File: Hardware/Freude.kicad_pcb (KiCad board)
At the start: 4 copper layers, 30 parts, among them J1 Conn_01x06_Female, J2 Conn_01x05_Female, J3 Conn_01x06_Female, J4 Conn_01x04_Female, J5 Conn_01x04_Female, J6 Conn_01x04_Male, U1 IQS572, U2 STM32L432KBUx, X1 Custom_Touchpad, Y1 Crystal_GND24

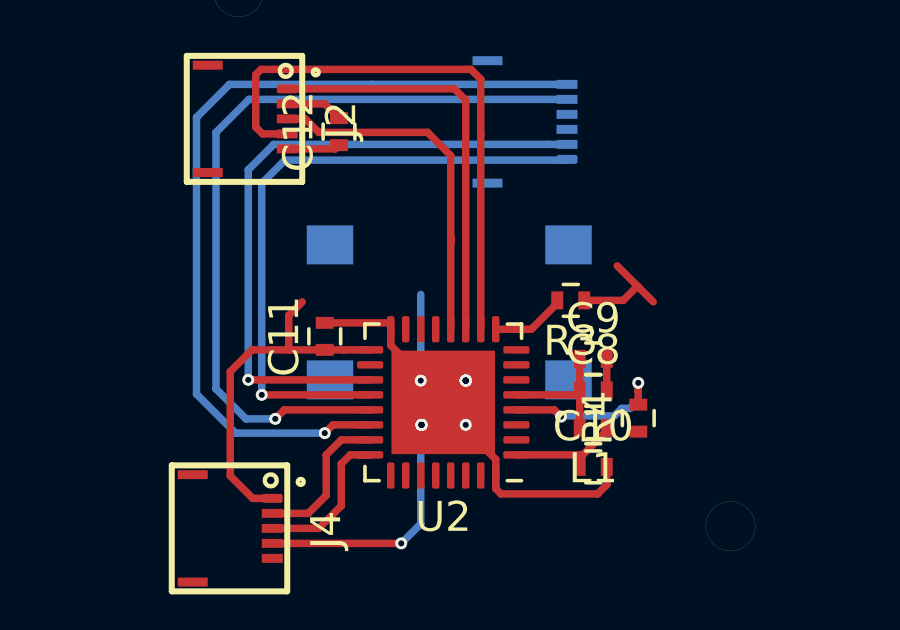
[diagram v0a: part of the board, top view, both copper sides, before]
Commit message: create part B3FS-1015p include 3d file. Add to PCB
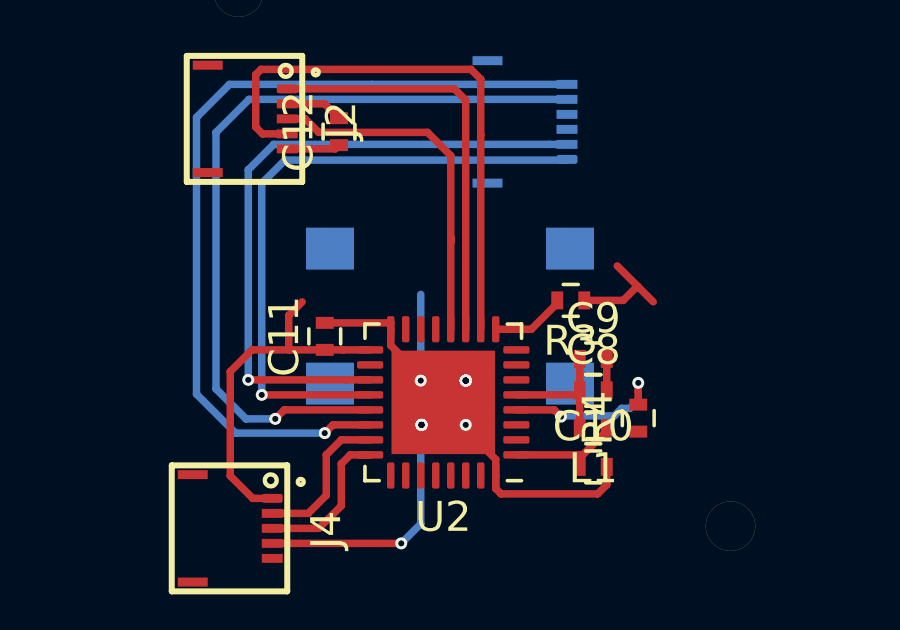
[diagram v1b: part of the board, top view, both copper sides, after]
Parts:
- removed the REF** at (200.7, 79.7)
- added REF**: B3FS-1015P, .pretty:B3FS-1015P, B.Cu at (200.7, 79.8)
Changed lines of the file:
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@@
     (35 F.Paste user hide)
     (37 F.SilkS user)
-    (39 F.Mask user)
+    (39 F.Mask user hide)
     (40 Dwgs.User user)
     (41 Cmts.User user)
@@
     (43 Eco2.User user)
     (44 Edge.Cuts user)
-    (45 Margin user)
+    (45 Margin user hide)
     (46 B.CrtYd user)
-    (47 F.CrtYd user)
+    (47 F.CrtYd user hide)
     (49 F.Fab user hide)
   )
@@
     )
   )
-  (module digikey-footprints:Switch_Tactile_SMD_6x6mm_PTS645 (layer B.Cu)
-    (at 200.7 79.7 180)
-    (descr http://www.ckswitches.com/media/1471/pts645.pdf)
-    (fp_text reference REF** (at 0 4.27 180) (layer B.SilkS)
-      (effects (font (size 1 1) (thickness 0.15)) (justify mirror))
-    )
-    (fp_text value Switch_Tactile_SMD_6x6mm_PTS645 (at 0 -4.5 180) (layer B.Fab)
-      (effects (font (size 1 1) (thickness 0.15)) (justify mirror))
-    )
-    (fp_line (start -3 3) (end 3 3) (layer B.Fab) (width 0.1))
-    (fp_line (start -3 -3) (end 3 -3) (layer B.Fab) (width 0.1))
-    (fp_line (start -3 3) (end -3 -3) (layer B.Fab) (width 0.1))
-    (fp_line (start 3 -3) (end 3 3) (layer B.Fab) (width 0.1))
-    (fp_line (start -3.1 0) (end -3.1 0.5) (layer B.SilkS) (width 0.1))
-    (fp_line (start -3.1 0) (end -3.1 -0.5) (layer B.SilkS) (width 0.1))
-    (fp_line (start 3.1 0) (end 3.1 0.5) (layer B.SilkS) (width 0.1))
-    (fp_line (start 3.1 0) (end 3.1 -0.5) (layer B.SilkS) (width 0.1))
-    (fp_line (start 0 -3.1) (end -0.5 -3.1) (layer B.SilkS) (width 0.1))
-    (fp_line (start 0 -3.1) (end 0.5 -3.1) (layer B.SilkS) (width 0.1))
-    (fp_line (start 0 3.1) (end 0.5 3.1) (layer B.SilkS) (width 0.1))
-    (fp_line (start 0 3.1) (end -0.5 3.1) (layer B.SilkS) (width 0.1))
-    (fp_line (start -3.4 3) (end -4.6 3) (layer B.SilkS) (width 0.1))
-    (fp_line (start -3.1 3) (end -3.4 3) (layer B.SilkS) (width 0.1))
-    (fp_line (start -3.1 3.1) (end -3.1 3) (layer B.SilkS) (width 0.1))
-    (fp_line (start -2.6 3.1) (end -3.1 3.1) (layer B.SilkS) (width 0.1))
-    (fp_text user %R (at 0 0 180) (layer B.Fab)
-      (effects (font (size 1 1) (thickness 0.15)) (justify mirror))
-    )
-    (fp_line (start 5 3.25) (end 5 -3.25) (layer B.CrtYd) (width 0.05))
-    (fp_line (start 5 3.25) (end -5 3.25) (layer B.CrtYd) (width 0.05))
-    (fp_line (start 5 -3.25) (end -5 -3.25) (layer B.CrtYd) (width 0.05))
-    (fp_line (start -5 3.25) (end -5 -3.25) (layer B.CrtYd) (width 0.05))
-    (pad 4 smd rect (at 3.975 -2.25 180) (size 1.55 1.3) (layers B.Cu B.Paste B.Mask))
-    (pad 3 smd rect (at -3.975 -2.25 180) (size 1.55 1.3) (layers B.Cu B.Paste B.Mask))
-    (pad 2 smd rect (at 3.975 2.25 180) (size 1.55 1.3) (layers B.Cu B.Paste B.Mask))
-    (pad 1 smd rect (at -3.975 2.25 180) (size 1.55 1.3) (layers B.Cu B.Paste B.Mask))
-  )
   (module Resistors_SMD:R_0402 (layer F.Cu)
     (at 207 83.225 90)
@@
     )
   )
+  (module .pretty:B3FS-1015P (layer B.Cu)
+    (at 200.725 79.825)
+    (fp_text reference REF** (at 0 -0.5) (layer B.SilkS)
+      (effects (font (size 1 1) (thickness 0.15)) (justify mirror))
+    )
+    (fp_text value B3FS-1015P (at 0 0.5) (layer B.Fab)
+      (effects (font (size 1 1) (thickness 0.15)) (justify mirror))
+    )
+    (fp_line (start -0.5 0) (end 0.5 0) (layer B.CrtYd) (width 0.2))
+    (fp_line (start 0 0.5) (end 0 -0.5) (layer B.CrtYd) (width 0.2))
+    (fp_line (start -3.15 -1.2) (end -3.15 1.2) (layer B.SilkS) (width 0.2))
+    (fp_line (start -2.8 3) (end 2.8 3) (layer B.SilkS) (width 0.2))
+    (fp_line (start 3.15 -1.2) (end 3.15 1.2) (layer B.SilkS) (width 0.2))
+    (fp_line (start -2.8 -3) (end 2.8 -3) (layer B.SilkS) (width 0.2))
+    (fp_line (start -3.15 -3) (end -3.15 3) (layer B.CrtYd) (width 0.2))
+    (fp_line (start 3.15 -3) (end 3.15 3) (layer B.CrtYd) (width 0.2))
+    (fp_line (start -3.15 -3) (end 3.15 -3) (layer B.CrtYd) (width 0.2))
+    (fp_line (start -3.15 3) (end 3.15 3) (layer B.CrtYd) (width 0.2))
+    (pad 4 smd rect (at -4 2.25) (size 1.6 1.4) (layers B.Cu B.Paste B.Mask))
+    (pad 3 smd rect (at 4 2.25) (size 1.6 1.4) (layers B.Cu B.Paste B.Mask))
+    (pad 2 smd rect (at -4 -2.25) (size 1.6 1.4) (layers B.Cu B.Paste B.Mask))
+    (pad 1 smd rect (at 4 -2.25) (size 1.6 1.4) (layers B.Cu B.Paste B.Mask))
+    (model ${KIPRJMOD}/.pretty/B3FS_1000.step
+      (at (xyz 0 0 0))
+      (scale (xyz 1 1 1))
+      (rotate (xyz -90 0 0))
+    )
+  )

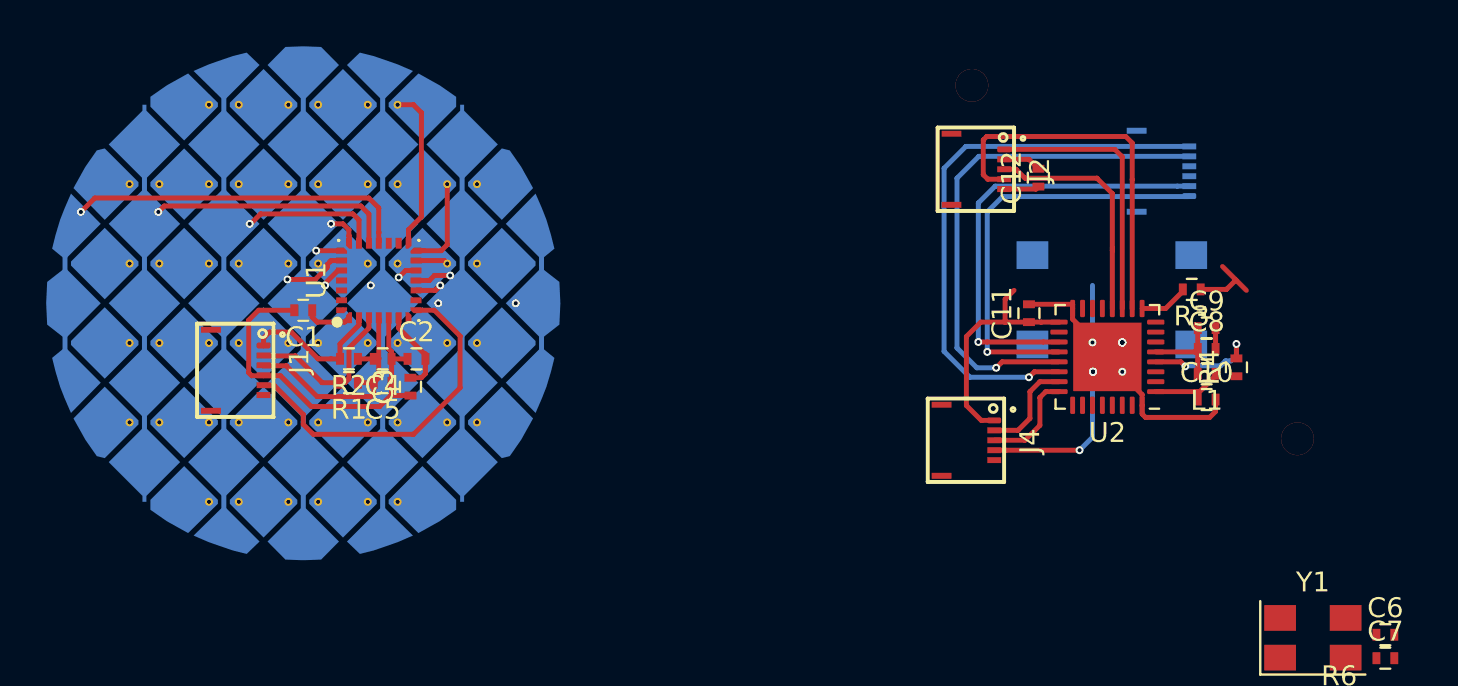
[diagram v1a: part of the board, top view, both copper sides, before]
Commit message: define boards edges
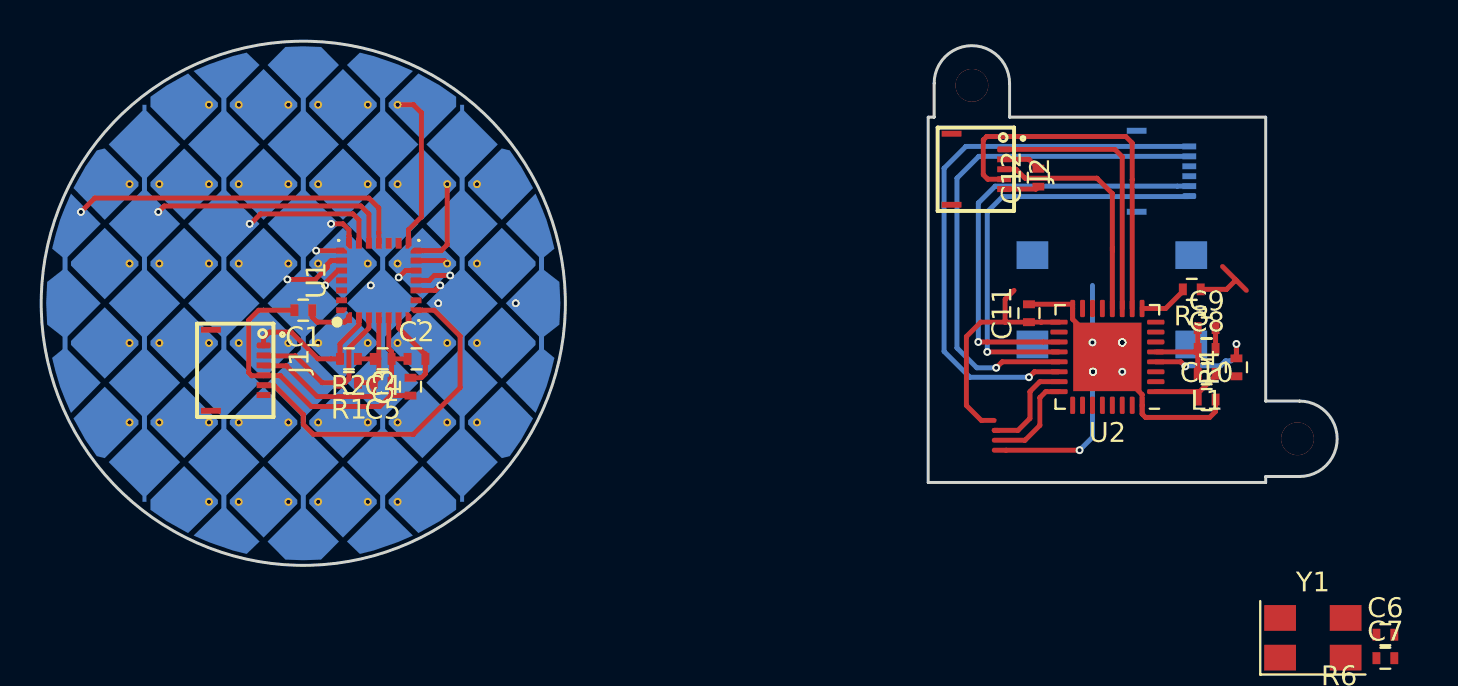
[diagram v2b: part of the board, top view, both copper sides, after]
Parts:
- removed J4: Conn_01x04_Female, .pretty:503480-0500
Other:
- board outline added: 65.3 x 26.4 mm
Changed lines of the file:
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@@
   (general
     (thickness 1.6)
-    (drawings 15)
+    (drawings 29)
     (tracks 329)
     (zones 0)
-    (modules 30)
+    (modules 29)
     (nets 63)
   )
@@
     (33 F.Adhes user hide)
     (35 F.Paste user hide)
-    (37 F.SilkS user)
+    (37 F.SilkS user hide)
     (39 F.Mask user hide)
     (40 Dwgs.User user)
@@
   )
   (module .pretty:503480-0500 (layer F.Cu)
-    (at 194.8 86.9 270)
-    (fp_text reference J4 (at 0.05 -1.8 270) (layer F.SilkS)
-      (effects (font (size 1 1) (thickness 0.15)))
-    )
-    (fp_text value Conn_01x04_Female (at 0 -0.5 270) (layer F.Fab)
-      (effects (font (size 1 1) (thickness 0.15)))
-    )
-    (fp_line (start -2.05 3.25) (end -2.05 -0.45) (layer F.CrtYd) (width 0.2))
-    (fp_line (start 2.05 3.25) (end -2.05 3.25) (layer F.CrtYd) (width 0.2))
-    (fp_line (start 2.05 -0.45) (end 2.05 3.25) (layer F.CrtYd) (width 0.2))
-    (fp_line (start -2.05 -0.45) (end 2.05 -0.45) (layer F.CrtYd) (width 0.2))
-    (fp_line (start 0 1.675) (end 0 2.675) (layer F.CrtYd) (width 0.2))
-    (fp_line (start -0.5 2.175) (end 0.5 2.175) (layer F.CrtYd) (width 0.2))
-    (fp_circle (center -1.6 0.05) (end -1.529289 0.05) (layer F.SilkS) (width 0.4))
-    (fp_circle (center -1.55 -0.95) (end -1.5 -0.9) (layer F.SilkS) (width 0.2))
-    (fp_line (start 2.1 3.35) (end 2.1 -0.5) (layer F.SilkS) (width 0.2))
-    (fp_line (start -2.1 -0.5) (end 2.1 -0.5) (layer F.SilkS) (width 0.2))
-    (fp_line (start -2.1 3.35) (end -2.1 -0.5) (layer F.SilkS) (width 0.2))
-    (fp_line (start -2.1 3.35) (end 2.1 3.35) (layer F.SilkS) (width 0.2))
-    (pad 0 smd rect (at 1.79 2.65 270) (size 0.3 1) (layers F.Cu F.Paste F.Mask))
-    (pad 0 smd rect (at -1.79 2.65 270) (size 0.3 1) (layers F.Cu F.Paste F.Mask))
-    (pad 5 smd rect (at 1 0 270) (size 0.3 0.7) (layers F.Cu F.Paste F.Mask))
-    (pad 4 smd rect (at 0.5 0 270) (size 0.3 0.7) (layers F.Cu F.Paste F.Mask)
-      (net 16 GND))
-    (pad 3 smd rect (at 0 0 270) (size 0.3 0.7) (layers F.Cu F.Paste F.Mask)
-      (net 42 /SWCLK))
-    (pad 2 smd rect (at -0.5 0 270) (size 0.3 0.7) (layers F.Cu F.Paste F.Mask)
-      (net 41 /SWDIO))
-    (pad 1 smd roundrect (at -1 0 270) (size 0.3 0.7) (layers F.Cu F.Paste F.Mask) (roundrect_rratio 0.25)
-      (net 15 +3V3))
-  )
-  (module .pretty:503480-0500 (layer F.Cu)
     (at 195.3 73.25 270)
     (fp_text reference J2 (at 0.05 -1.8 270) (layer F.SilkS)
@@
     )
   )
+  (gr_circle (center 160 80) (end 160 66.8) (layer Edge.Cuts) (width 0.15))
+  (gr_line (start 191.475 70.625) (end 191.475 89.025) (layer Edge.Cuts) (width 0.15))
+  (gr_line (start 191.775 70.625) (end 191.475 70.625) (layer Edge.Cuts) (width 0.15))
+  (gr_line (start 191.775 70.625) (end 191.775 68.925) (layer Edge.Cuts) (width 0.15))
+  (gr_arc (start 193.675 68.925) (end 195.575 68.925) (angle -180) (layer Edge.Cuts) (width 0.15))
+  (gr_line (start 195.575 70.625) (end 195.575 68.925) (layer Edge.Cuts) (width 0.15))
+  (gr_line (start 208.475 70.625) (end 195.575 70.625) (layer Edge.Cuts) (width 0.15))
+  (gr_line (start 208.475 84.925) (end 208.475 70.625) (layer Edge.Cuts) (width 0.15))
+  (gr_line (start 208.475 84.925) (end 210.175 84.925) (layer Edge.Cuts) (width 0.15))
+  (gr_arc (start 210.175 86.825) (end 210.175 88.725) (angle -180) (layer Edge.Cuts) (width 0.15))
+  (gr_line (start 208.475 88.725) (end 210.175 88.725) (layer Edge.Cuts) (width 0.15))
+  (gr_line (start 208.475 89.025) (end 208.475 88.725) (layer Edge.Cuts) (width 0.15))
+  (gr_line (start 208.45 89.025) (end 208.475 89.025) (layer Edge.Cuts) (width 0.15))
+  (gr_line (start 191.475 89.025) (end 208.45 89.025) (layer Edge.Cuts) (width 0.15))
   (gr_circle (center 160 80) (end 173 80) (layer Dwgs.User) (width 0.2))
   (gr_circle (center 160 80) (end 173 80) (layer Dwgs.User) (width 0.2))

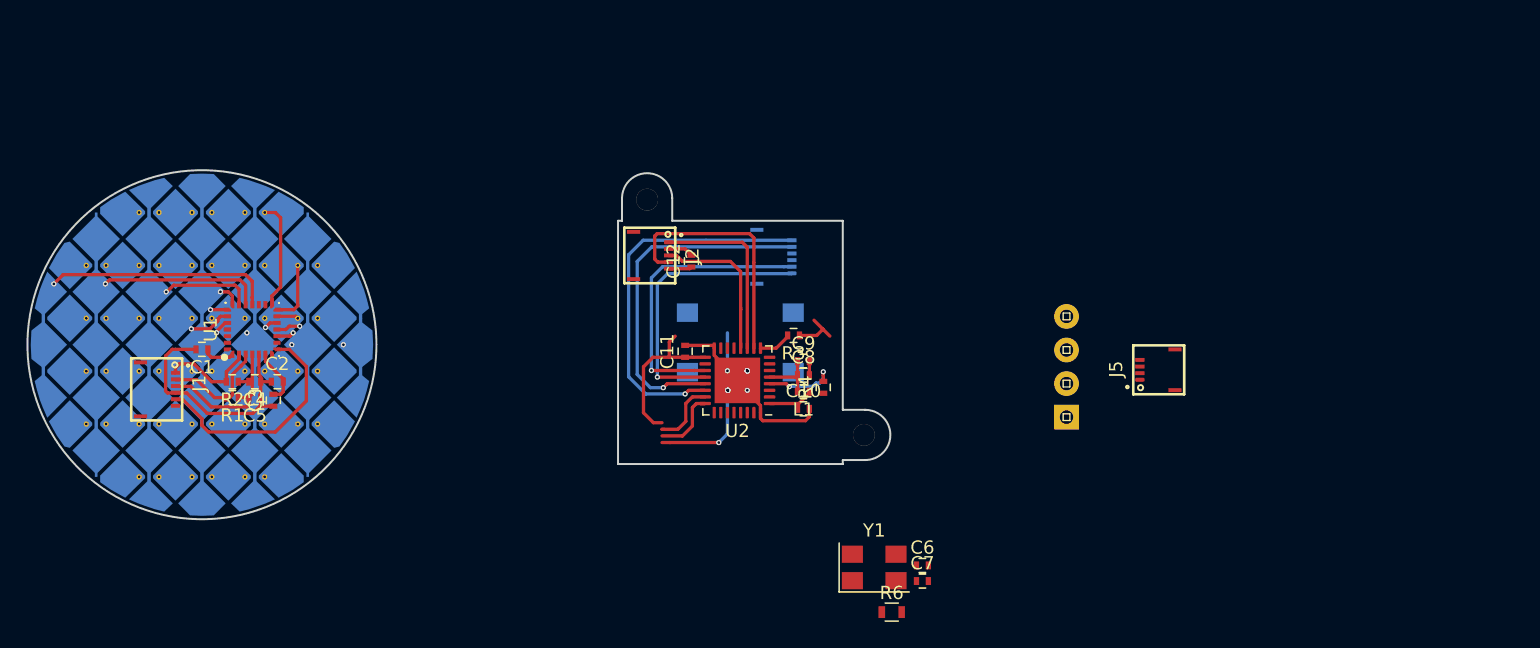
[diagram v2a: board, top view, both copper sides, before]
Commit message: added connectors for debug board.
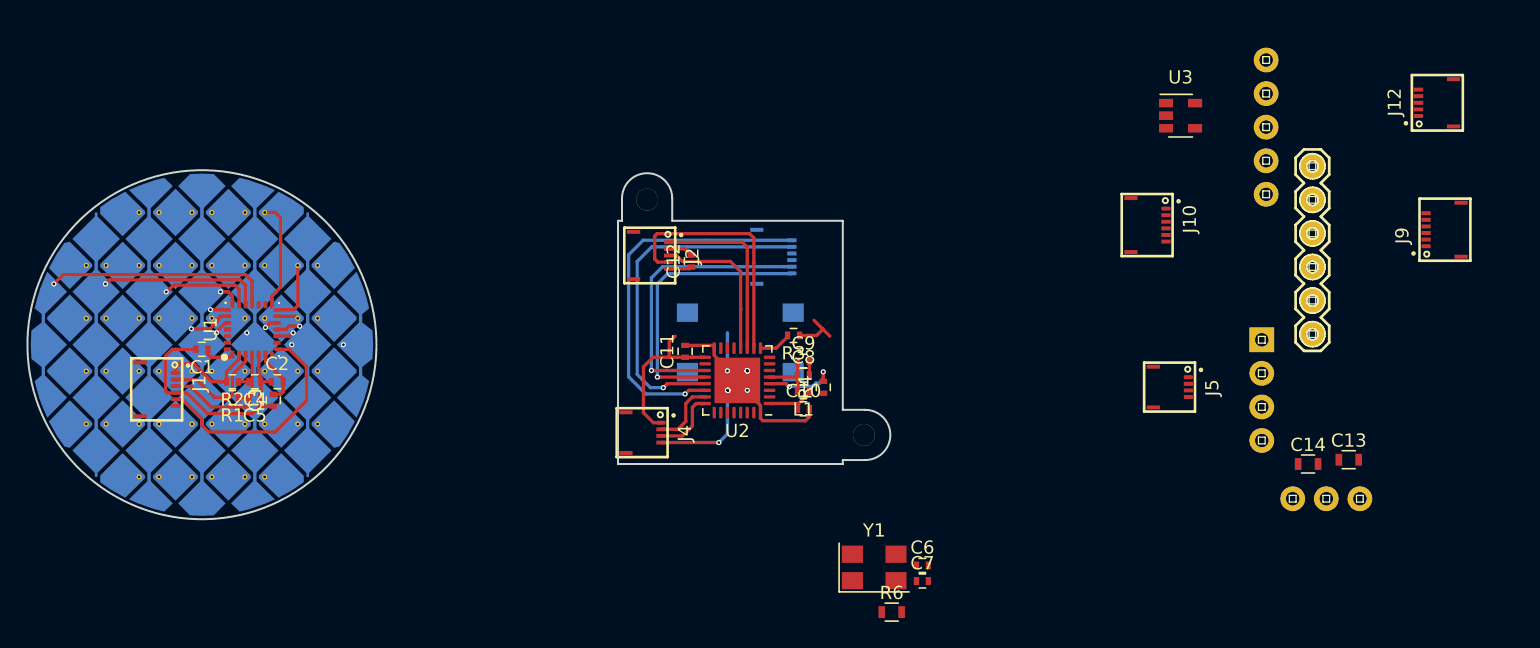
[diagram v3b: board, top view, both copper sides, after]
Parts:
- added C13: 0.1uf, Resistors_SMD:R_0603, F.Cu at (246.8, 88.7)
- added C14: 0.1uf, Resistors_SMD:R_0603, F.Cu at (243.7, 89.0)
- added J10: Conn_01x06_Female, .pretty:503480-0600, F.Cu at (232.9, 71.0)
- added J11: Conn_01x05_Male, SparkFun-Connectors:1X05, F.Cu at (240.5, 68.6)
- added J12: Conn_01x05_Female, .pretty:503480-0500, F.Cu at (252.0, 61.7)
- added J4: Conn_01x04_Female, .pretty:503480-0400, F.Cu at (194.7, 86.7)
- added J7: Conn_01x03_Female, SparkFun-Connectors:1X03, F.Cu at (247.6, 91.7)
- added J8: Conn_01x06_Male, SparkFun-Connectors:1X06-KIT, F.Cu at (244.0, 79.2)
- added J9: Conn_01x06_Female, .pretty:503480-0600, F.Cu at (252.6, 71.3)
- added U3: TLV713185PDBV, Package_TO_SOT_SMD:SOT-23-5, F.Cu at (234.0, 62.7)
- moved J6 15.9 mm to (240.2, 79.6), turned to 270 degrees
- moved J5 3.89 mm to (234.6, 83.2), turned to 270 degrees
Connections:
- net /Prog_VCC renamed +1V8
- J1 pad 6: (no net) -> Net-(J1-Pad6)
- J5 pad 4: /Prog_GND -> GNDA
- J6 pad 4: /Prog_GND -> GNDA
- U1 pad 1: Net-(C1-Pad1) -> Net-(U1-Pad1)
